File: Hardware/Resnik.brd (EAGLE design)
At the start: 64.8 x 100 mm, 172 parts, among them IC1 ATMEGA644M, J1 CONN_82.54_SCREW, J3 CONN_82.54_SCREW, J4 CONN_42.54_SCREW, Q1 DMG3404, Q2 DMG3404, Q3 FDN360P, Q4 FDN360P, Q5 FDN360P, Q6 DMG3404, U1 TLV61220DBV, U10 SN74AUP1G04YFP, U11 SN74AUP2G86SOT833-1, U12 SN74AUP2G08DQE, U13 SN74AUP2G08DQE, U14 SN74AUP2G08DQE, U15 MIC2039MT, U16 MIC2039MT, U17 MIC2039MT, U18 MIC2039MT, U19 TPS22917DBV, U2 TPS62822DLC, U20 TPS22917DBV, U21 TXS0102DQM, U22 BME280, U23 FT231X-Q, U24 TPS22917DBV, U25 TXS0108RGY, U26 TXS0108RGY, U27 TXS0104RGY, U28 MCP4726A2SOT-23, U29 ADS1115, U3 TPS61032RSA, U30 ADS1115, U31 INA211DCK, U32 INA210DCK, U33 TCA9555RTW, U5 BQ2980RUG, U6 TPS2105, U7 LTC4412S6, U8 TPS79733, U9 SN74AUP1G04YFP

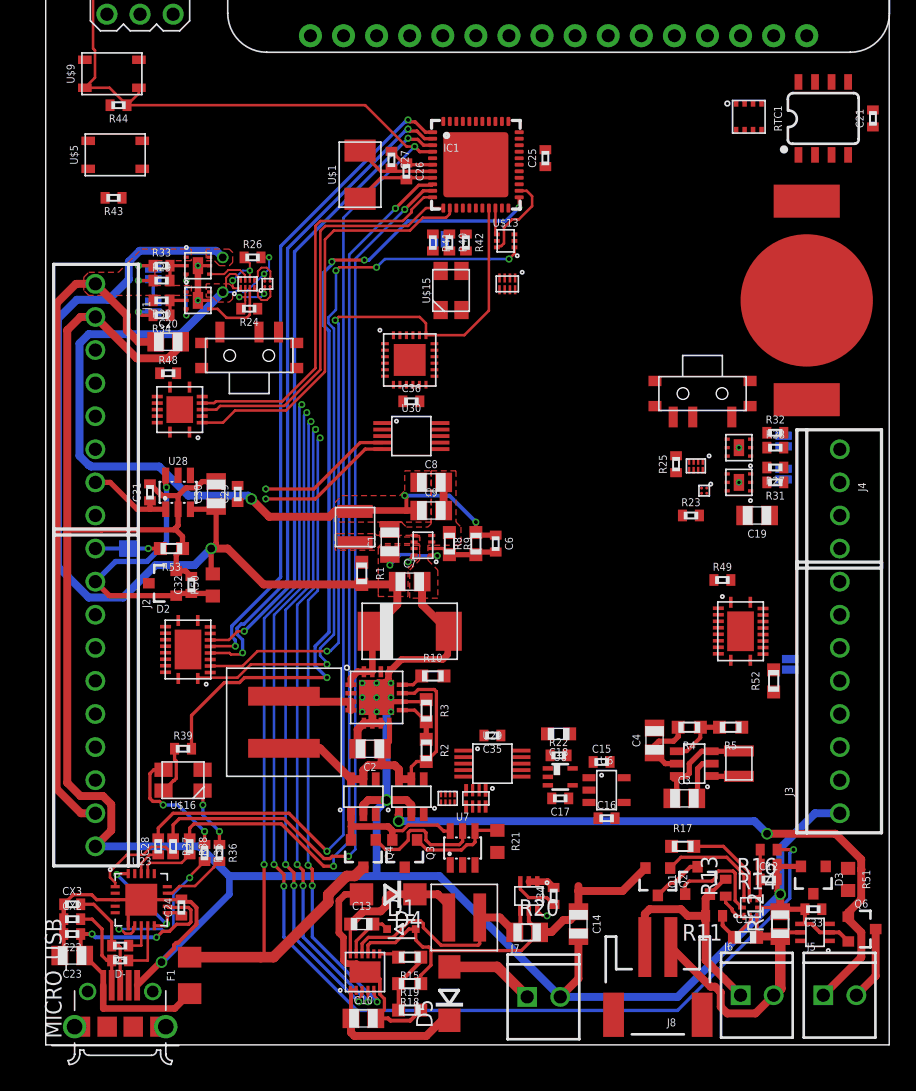
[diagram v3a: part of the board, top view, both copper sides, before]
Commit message: Continued layout, major of power and prime bus done
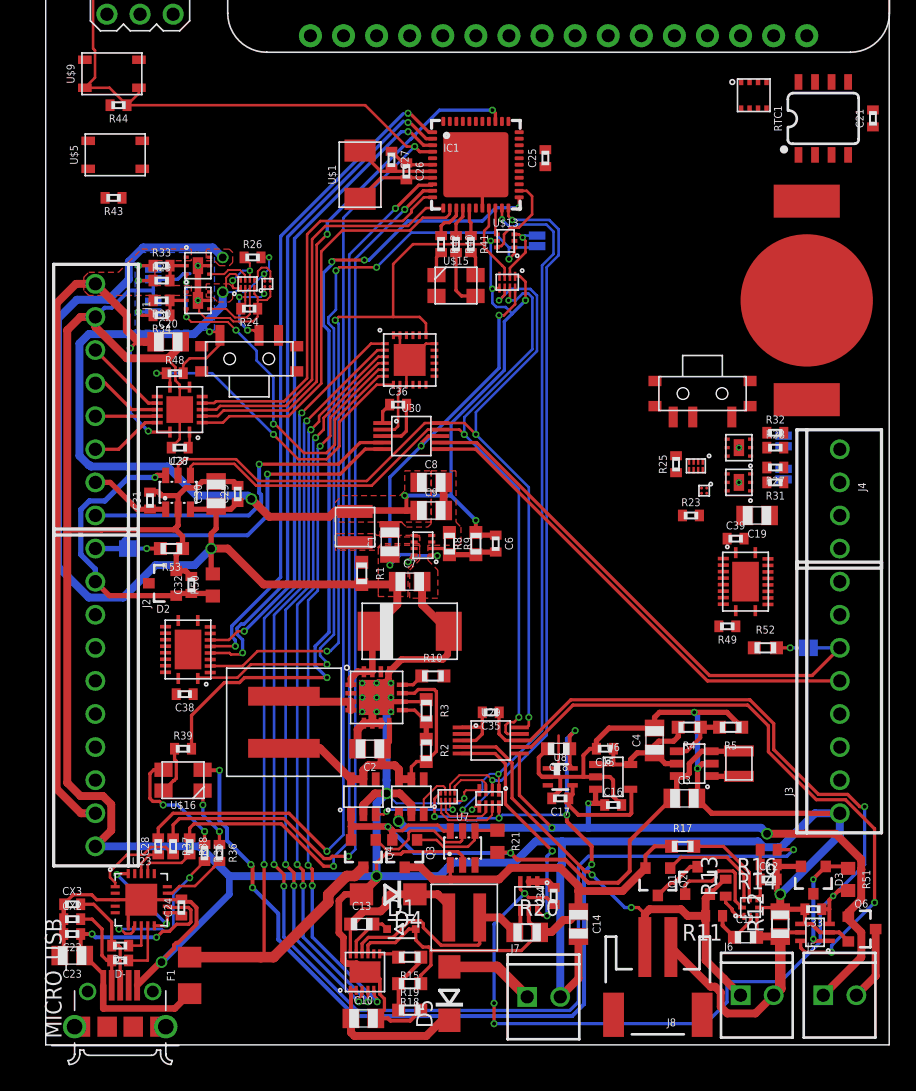
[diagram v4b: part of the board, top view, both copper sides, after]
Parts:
- removed R22: 10k, bschulz_passives:R0402
- added C37, C38, C39: (no value), bschulz_passives:C0402
- moved JP5 7.49 mm to (37.7, 61.7), turned to 270 degrees
- moved U26 3.83 mm to (53.7, 35.6)
- moved R49 3.58 mm to (52.3, 32.1), turned to 180 degrees
- moved R41 2.92 mm to (32.6, 61.5)
- moved R52 2.62 mm to (55.2, 30.5), turned to 0 degrees
- moved R42 1.91 mm to (30.4, 61.5)
- moved JP6 1.89 mm to (58.5, 30.5), turned to 0 degrees
- moved C35 1.78 mm to (34.2, 25.5)
- moved U29 1.78 mm to (34.2, 23.4)
- moved U22 1.69 mm to (54.4, 72.9)
- moved C18 1.14 mm to (39.4, 22.7)
- moved U6 1.14 mm to (43.6, 20.6)
- moved C16 1.14 mm to (43.6, 18.4)
- moved C15 1.05 mm to (42.9, 22.7), turned to 180 degrees
- moved C36 1.05 mm to (27.1, 49.1)
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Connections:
- net VBAT+ renamed V_CORE
- removed net 3V3: C25.1, IC1.17, IC1.27, IC1.29, IC1.38, IC1.5, ISP2.2, R44.2, U$16.2
- new net N$1: IC1.35
- net 3V3_AUX: now also C37.1, C38.1, C39.1
- net 3V3_CORE: now also C25.1, IC1.17, IC1.27, IC1.29, IC1.38, IC1.5, ISP2.2, R44.2, U$16.2; no longer R22.2
- net ADC_0: now also U30.5; no longer U30.4
- net ADC_1: now also U30.4; no longer U30.5
- net ADC_EXT_ALERT: now also U33.8
- net BMS_CTR: now also U33.2
- net BUS_LOGIC_EN_PRIME: now also U33.7
- net FAULT_PRIME: now also U33.6
- net GND: now also C37.2, C38.2, C39.2
- net GPIO_1: now also IC1.36
- net I_LI: now also U29.7; no longer U29.6
- net I_SOLAR: now also U29.5; no longer U29.4
- net LI+: now also U29.4; no longer U29.5
- net MPPT_CHRG: now also U33.4
- net MPPT_FAULT: now also U33.5
- net MPPT_SHDN: now also U33.3
- net PG_LDO: no longer R22.1
- net SDA: no longer U21.2
- net SDA_OB: now also U21.2
- net VUSB_POWER: now also U33.1
- net V_PRIME: now also U29.6; no longer U29.7
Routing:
- net GND: track 287.5 -> 410.2 mm, vias 4 -> 8
- net 5V_AUX: track 91.8 -> 214.3 mm, vias 4 -> 11
- net 3V3_CORE: track 0.00 -> 81.4 mm, vias 0 -> 8
- net SCL_5V: track 0.00 -> 68.7 mm, vias 0 -> 3
- net SDA_5V: track 0.00 -> 66.6 mm, vias 0 -> 3
- net C0: track 0.00 -> 59.5 mm, vias 0 -> 3
- net C1: track 0.00 -> 58.4 mm, vias 0 -> 3
- net I_LI: track 0.00 -> 47.6 mm, vias 0 -> 2
- net ADC_3: track 0.00 -> 41.0 mm
- net GPIO_1: track 0.00 -> 39.7 mm, vias 0 -> 2
- net ADC_2: track 0.00 -> 38.1 mm
- net 3V3_AUX: track 68.5 -> 104.3 mm, vias 6 -> 10
- net V_BETA: track 19.0 -> 47.4 mm, vias 0 -> 2
- net BUS_LOGIC_EN_PRIME: track 0.00 -> 26.3 mm, vias 0 -> 2
- net FAULT_PRIME: track 3.66 -> 29.6 mm, vias 2 -> 4
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- added copper zone on layer 16, net GND

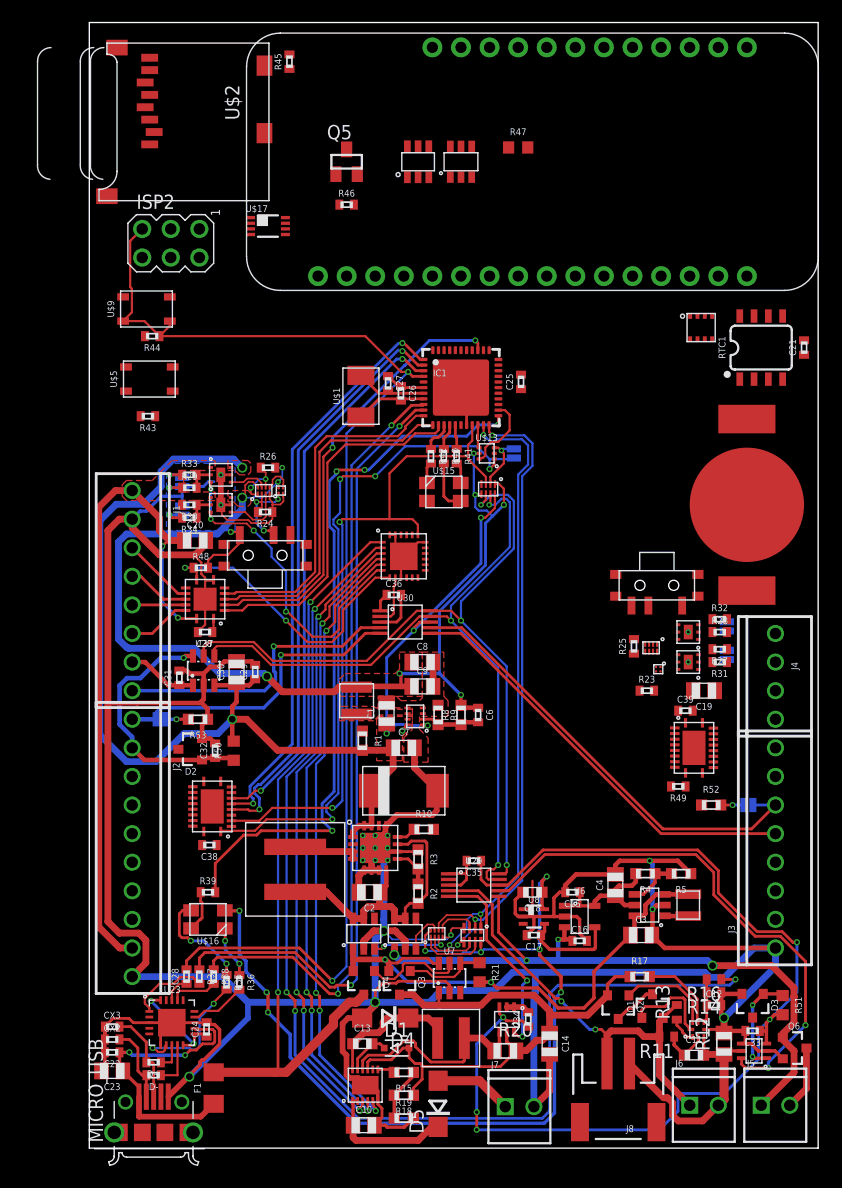
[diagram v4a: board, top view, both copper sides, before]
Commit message: Continued layout, majority of secondary bus, low power
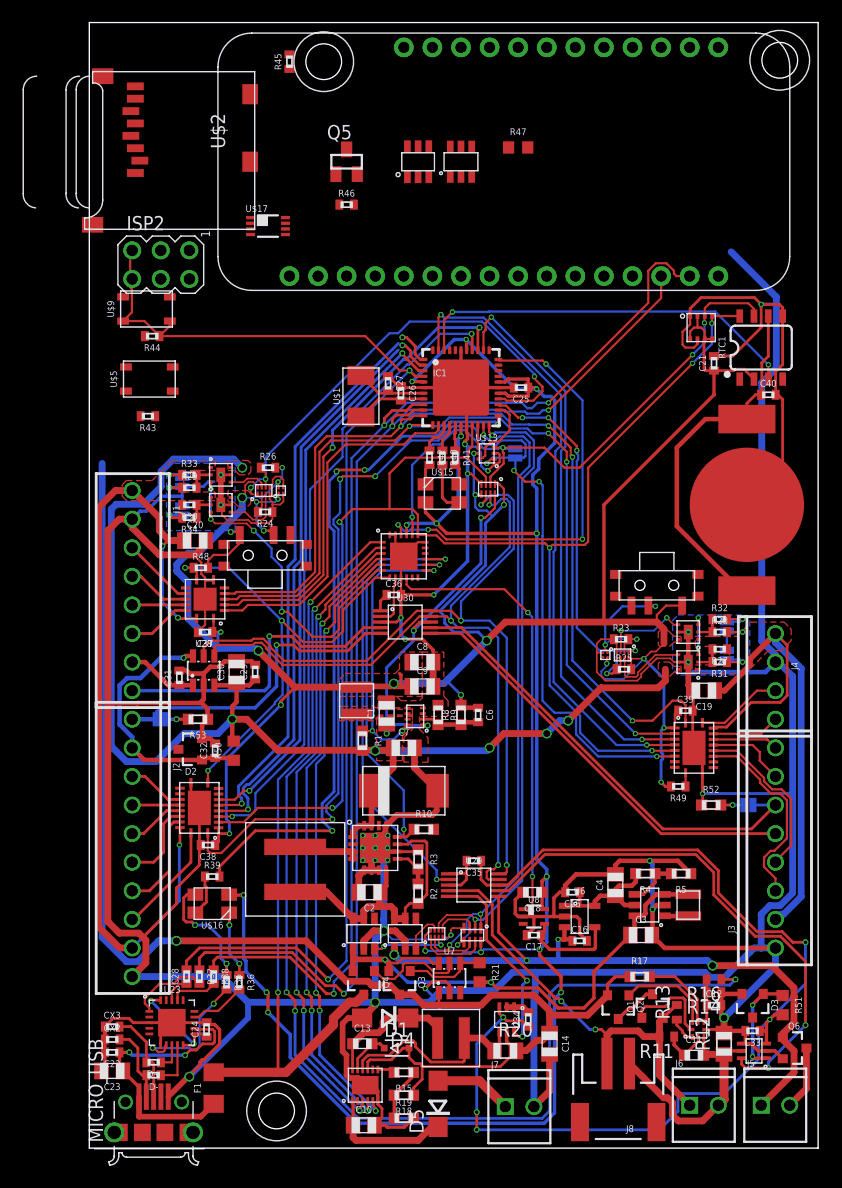
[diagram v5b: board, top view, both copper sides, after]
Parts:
- added C40: (no value), bschulz_passives:C0402
- added H1, H2, H3: (no value), bschulz:4_40
- moved C21 8.12 mm to (55.5, 69.7)
- moved R23 5.11 mm to (47.2, 45.2)
- moved U9 4.87 mm to (45.8, 43.8)
- moved U$2 2.84 mm to (14.7, 95.6)
- moved U12 2.62 mm to (47.4, 43.8)
- moved MS1 2.54 mm to (11.4, 76.2)
- moved R25 2.22 mm to (47.5, 42.5), turned to 0 degrees
- moved ISP2 2.10 mm to (6.35, 78.5)
- moved R39 1.45 mm to (10.9, 24.1)
- moved U$16 1.45 mm to (10.9, 21.7)
- moved U25 1.15 mm to (9.78, 30.2)
- moved C25 0.51 mm to (38.4, 67.6), turned to 180 degrees
- moved R41 0.18 mm to (32.5, 61.3)
- moved R42 0.18 mm to (30.2, 61.3)
- moved R40 0.18 mm to (31.4, 61.3)
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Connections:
- removed net N$1: IC1.35
- new net FAULT_SEC: U15.3, U16.3
- net 3V3_AUX_PG: now also U33.13
- net ADC_OB_ALERT: now also U33.15
- net CS_EXT: now also IC1.37
- net EN_BUS_PRIME: now also IC1.26; no longer IC1.25
- net EN_BUS_SEC: now also IC1.25; no longer IC1.26
- net FAULT_PRIME: no longer U15.3, U16.3
- net GLOBAL_INT: now also IC1.33; no longer IC1.34
- net GND: now also C40.2
- net GPIO_3: now also IC1.35
- net LBI: now also U33.14
- net LOG_INT: now also IC1.34; no longer IC1.33
- net N$43: now also C40.1
- net PG_LDO: now also U33.10
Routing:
- net GND: track 410.2 -> 630.3 mm, vias 8 -> 18
- net 3V3_AUX: track 104.3 -> 203.5 mm, vias 10 -> 18
- net 3V3_CORE: track 81.4 -> 177.3 mm, vias 8 -> 15
- net V_LI: track 51.6 -> 123.8 mm, vias 0 -> 1
- net SCL: track 61.4 -> 132.4 mm, vias 2 -> 6
- net CS_EXT: track 0.00 -> 57.0 mm, vias 0 -> 2
- net GPIO_2: track 0.00 -> 55.7 mm, vias 0 -> 2
- net RX_EXT: track 30.8 -> 81.5 mm, vias 0 -> 4
- net GPIO_3: track 0.00 -> 50.4 mm, vias 0 -> 2
- net VBUS_SEC: track 0.00 -> 49.0 mm
- net SDA_OB: track 5.48 -> 53.7 mm, vias 1 -> 4
- net SDA_EXT: track 60.8 -> 108.9 mm, vias 4 -> 7
- net TX_EXT: track 31.2 -> 77.8 mm, vias 0 -> 4
- net ADC_OB_ALERT: track 0.00 -> 40.4 mm, vias 0 -> 2
- net GLOBAL_INT: track 0.00 -> 39.3 mm, vias 0 -> 4
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- added copper zone on layer 1, net VBUS_SEC

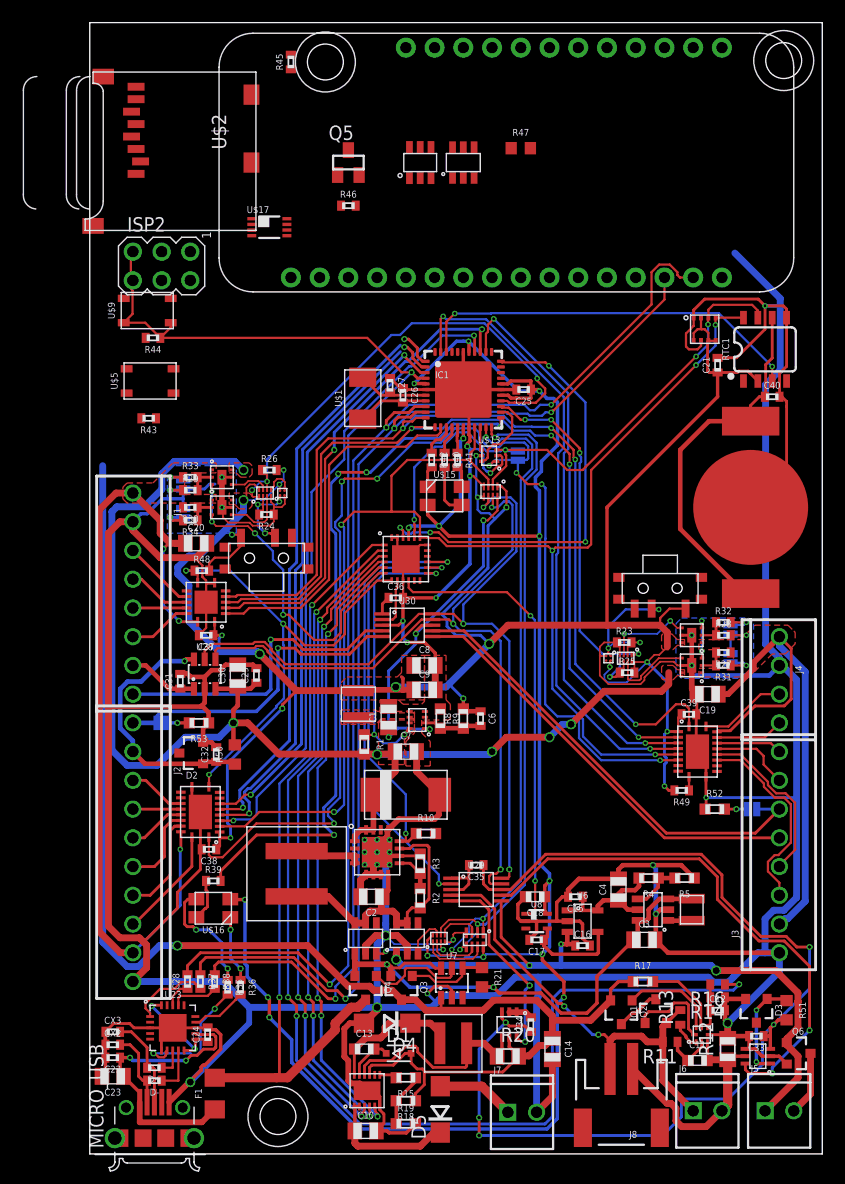
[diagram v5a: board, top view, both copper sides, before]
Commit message: Continued layout, starting on SD and Feather header
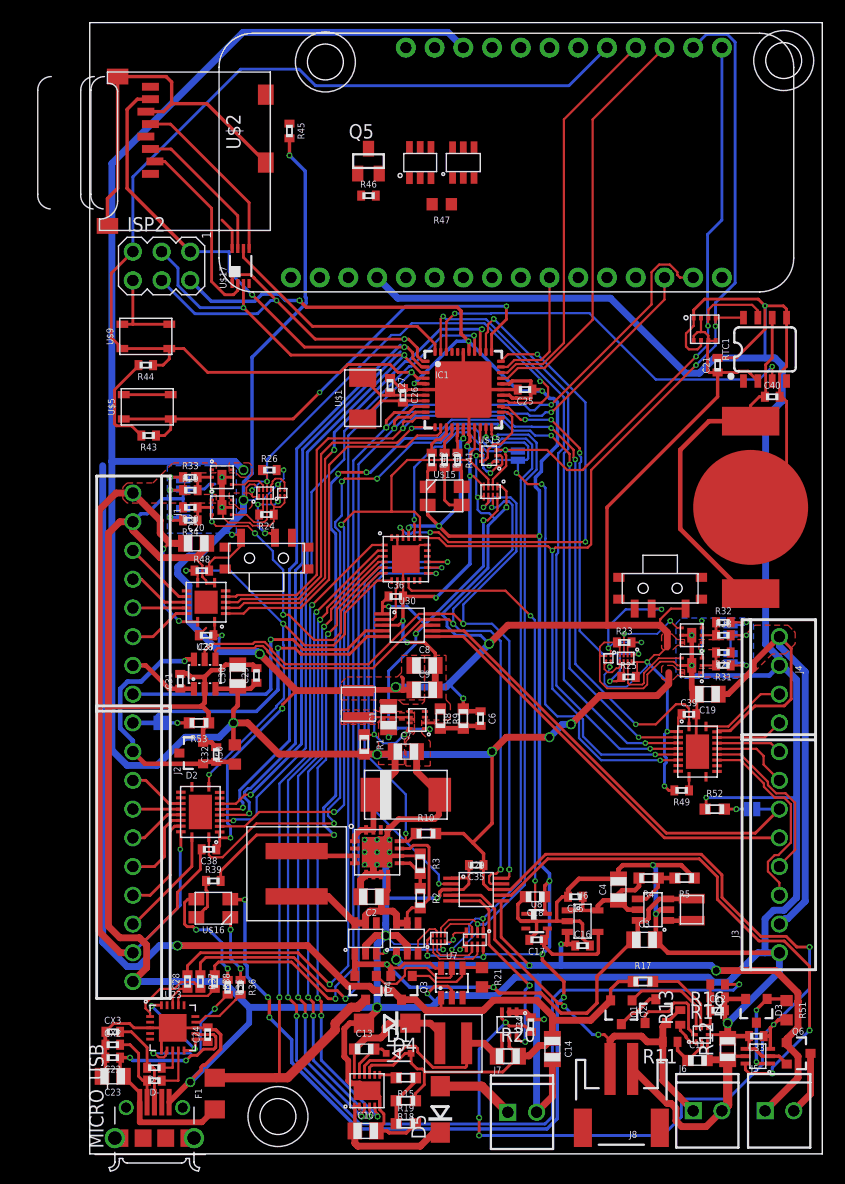
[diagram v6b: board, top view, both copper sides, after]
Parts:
- moved R47 8.56 mm to (31.1, 83.9), turned to 180 degrees
- moved R45 6.10 mm to (17.7, 90.4), turned to 270 degrees
- moved U$17 4.27 mm to (13.3, 78.5), turned to 0 degrees
- moved R44 2.50 mm to (4.95, 69.7)
- moved U$5 2.30 mm to (5.08, 66.0)
- moved U$9 2.29 mm to (4.95, 72.3)
- moved R46 1.99 mm to (24.6, 84.7)
- moved Q5 1.78 mm to (24.6, 87.8)
- moved R43 1.52 mm to (5.21, 63.5)
- moved U$2 1.27 mm to (16.0, 95.6)
- moved R25 0.40 mm to (47.6, 42.2)
- moved C25 0.13 mm to (38.5, 67.6)
- moved C36 0.13 mm to (27.1, 49.3)
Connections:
- net MOSI: now also U$17.1; no longer U$17.3
- net MOSI_BUF: now also U$17.7; no longer U$17.5
- net SCK: now also U$17.3; no longer U$17.1
- net SCK_BUF: now also U$17.5; no longer U$17.7
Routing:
- net 5V_AUX: track 243.9 -> 327.8 mm, vias 15 -> 16
- net GND: track 630.3 -> 703.0 mm, vias 18 -> 20
- net RST: track 109.2 -> 167.3 mm
- net LOG_INT: track 0.00 -> 45.0 mm, vias 0 -> 2
- net MISO: track 52.4 -> 93.2 mm, vias 2 -> 3
- net 3V3_AUX: track 203.5 -> 242.0 mm, vias 18 -> 19
- net 3V3_CORE: track 177.3 -> 215.1 mm, vias 15 -> 16
- net FEATHER_RTS: track 0.00 -> 36.9 mm
- net FEATHER_CTS: track 0.00 -> 35.4 mm
- net SCL: track 132.4 -> 162.7 mm
- net MOSI: track 52.1 -> 82.2 mm, vias 2 -> 3
- net SCK: track 50.1 -> 78.4 mm, vias 2 -> 3
- net SDA_OB: track 53.7 -> 78.8 mm
- net SD_CS: track 0.00 -> 21.6 mm
- net SD_CS_BUF: track 0.00 -> 16.8 mm
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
